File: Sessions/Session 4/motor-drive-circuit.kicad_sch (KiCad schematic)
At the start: 13 parts, among them M2 Drive Motor, Q1 IRF540N, Q2 IRF9540N, Q3 IRLZ44N, Q4 IRF40DM229, Q5 IRF9540N, Q6 IRF540N

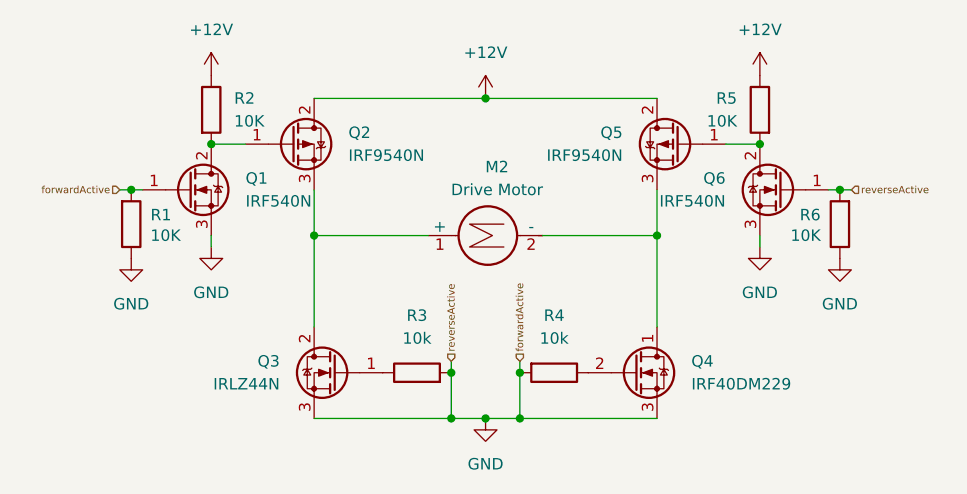
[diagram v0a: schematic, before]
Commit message: Fixed schematic mistake
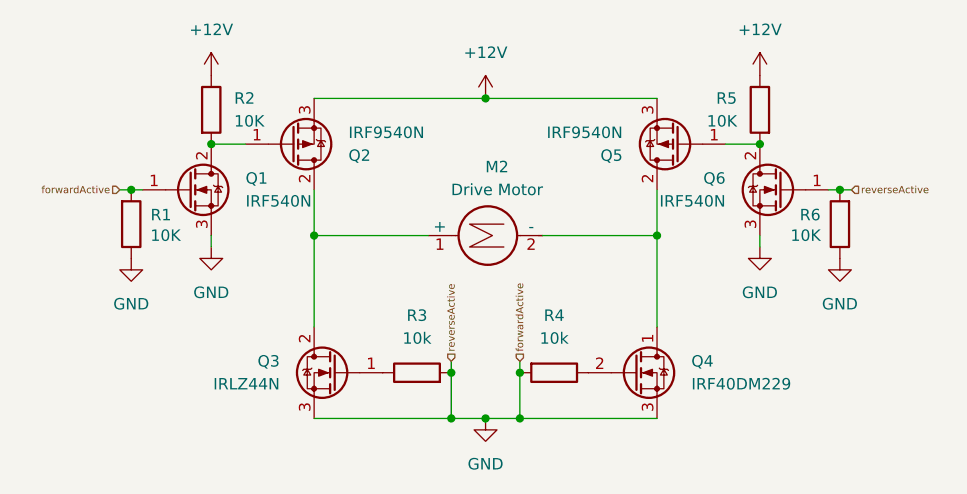
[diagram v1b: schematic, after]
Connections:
- net +12V: now also Q2.3 (S), Q5.3 (S); no longer Q2.2 (D), Q5.2 (D)
- net at M2.2 (-), Q4.1 (D): now also Q5.2 (D); no longer Q5.3 (S)
- net at M2.1 (+), Q3.2 (D): now also Q2.2 (D); no longer Q2.3 (S)
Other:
- moved on the sheet: Q5
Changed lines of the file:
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@@
 	(symbol
 		(lib_id "Transistor_FET:IRF9540N")
-		(at 161.29 83.82 0)
-		(mirror y)
+		(at 161.29 83.82 180)
 		(unit 1)
 		(exclude_from_sim no)
@@
 		(dnp no)
 		(property "Reference" "Q5"
-			(at 154.94 82.5499 0)
+			(at 154.94 85.0901 0)
 			(effects
 				(font
@@
 		)
 		(property "Value" "IRF9540N"
-			(at 154.94 85.0899 0)
+			(at 154.94 82.5501 0)
 			(effects
 				(font
@@
 		)
 		(property "Footprint" "Package_TO_SOT_THT:TO-220-3_Vertical"
-			(at 156.21 85.725 0)
+			(at 156.21 81.915 0)
 			(effects
 				(font
@@
 		)
 		(property "Datasheet" "http://www.irf.com/product-info/datasheets/data/irf9540n.pdf"
-			(at 156.21 87.63 0)
+			(at 156.21 80.01 0)
 			(effects
 				(font
@@
 		(lib_id "Transistor_FET:IRF9540N")
 		(at 118.11 83.82 0)
-		(unit 1)
-		(exclude_from_sim no)
-		(in_bom yes)
-		(on_board yes)
-		(dnp no)
-		(fields_autoplaced yes)
+		(mirror x)
+		(unit 1)
+		(exclude_from_sim no)
+		(in_bom yes)
+		(on_board yes)
+		(dnp no)
 		(property "Reference" "Q2"
-			(at 124.46 82.5499 0)
+			(at 124.46 85.0901 0)
 			(effects
 				(font
@@
 		)
 		(property "Value" "IRF9540N"
-			(at 124.46 85.0899 0)
+			(at 124.46 82.5501 0)
 			(effects
 				(font
@@
 		)
 		(property "Footprint" "Package_TO_SOT_THT:TO-220-3_Vertical"
-			(at 123.19 85.725 0)
+			(at 123.19 81.915 0)
 			(effects
 				(font
@@
 		)
 		(property "Datasheet" "http://www.irf.com/product-info/datasheets/data/irf9540n.pdf"
-			(at 123.19 87.63 0)
-			(effects
-				(font
+			(at 123.19 80.01 0)
+			(effects
+				(font
